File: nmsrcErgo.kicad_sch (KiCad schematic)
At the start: 56 parts, among them SW1 RotaryEncoder_Switch, U1 Nice_Nano_V2

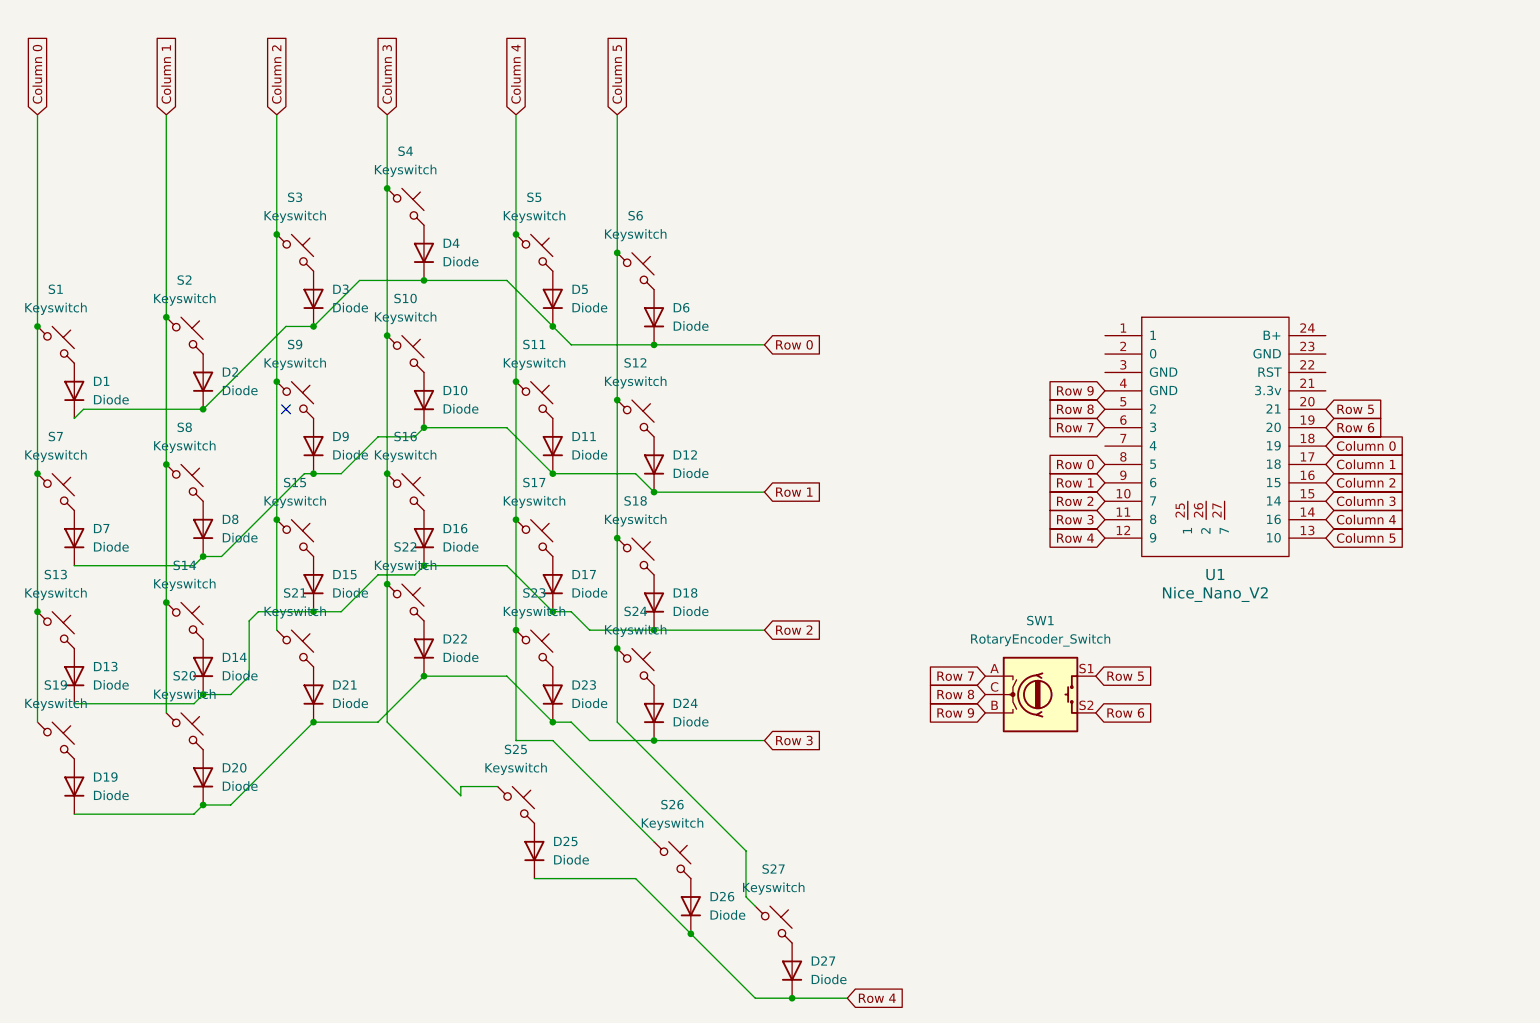
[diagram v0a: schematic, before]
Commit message: on/off switch and fixed encoder. added battery solder pads
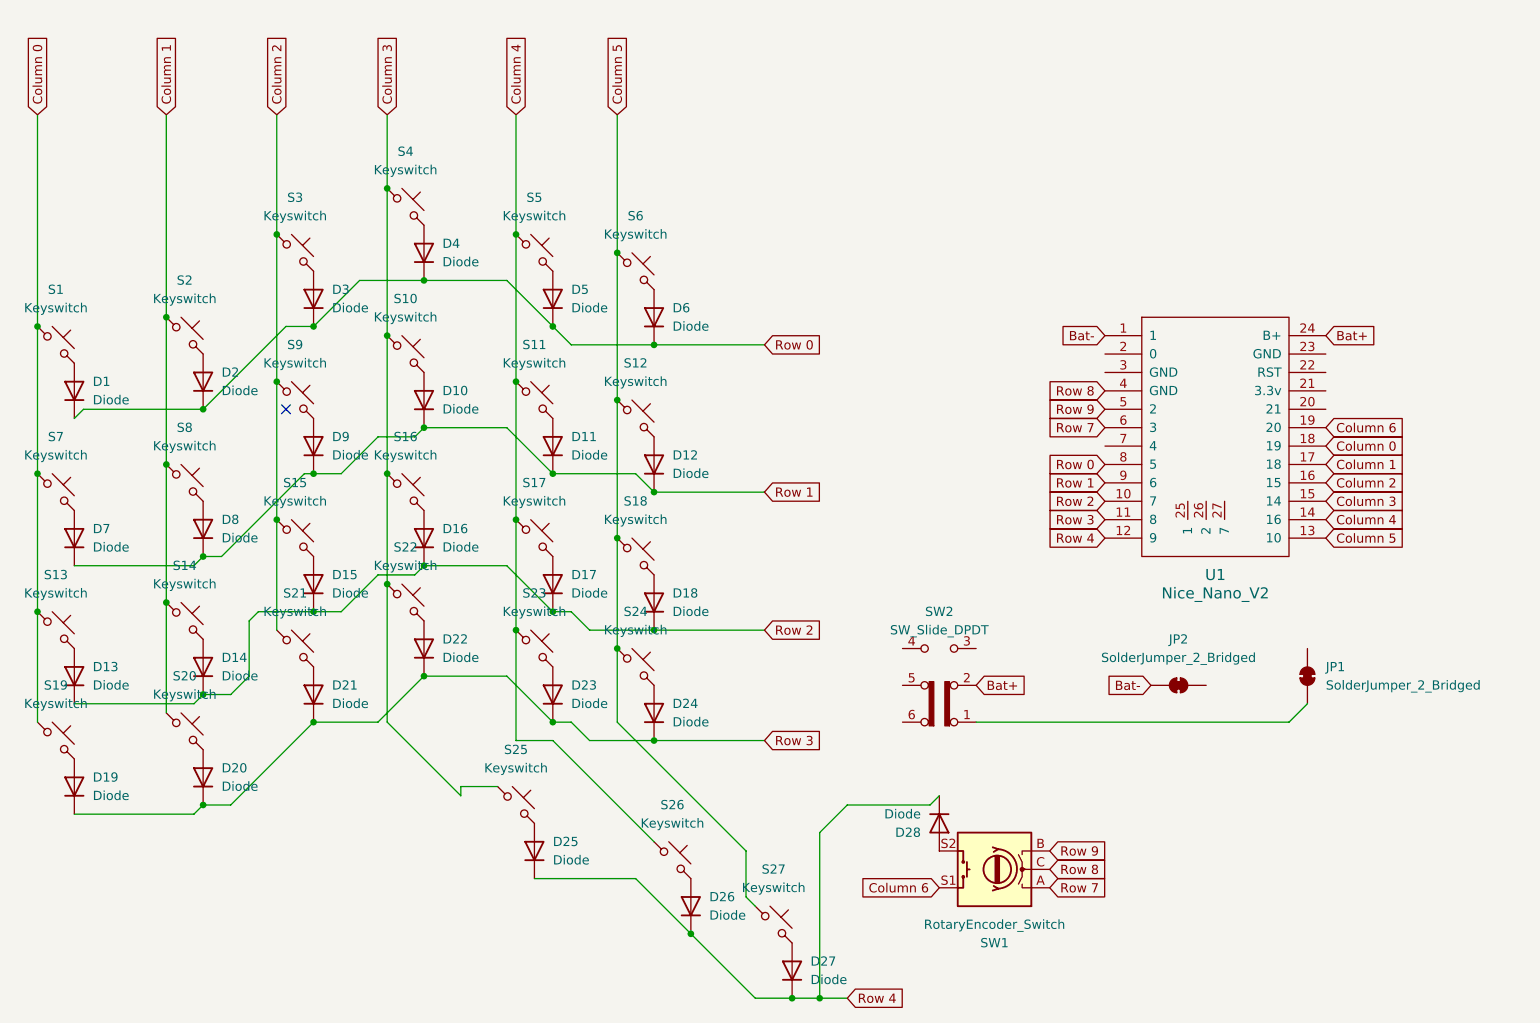
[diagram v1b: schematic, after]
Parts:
- added D28: Diode, ScottoKeebs_Components:Diode_DO-35, symbol ScottoKeebs:Placeholder_Diode
- added JP1, JP2: SolderJumper_2_Bridged, ScottoKeebs_Miscellaneous:solderpadv2, symbol Jumper:SolderJumper_2_Bridged
- added SW2: SW_Slide_DPDT, Button_Switch_THT:SW_Slide-03_Wuerth-WS-SLTV_10x2.5x6.4_P2.54mm, symbol Switch:SW_Slide_DPDT
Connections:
- net Row 4: now also D28.1 (K)
- net Row 8: now also U1.4 (GND); no longer U1.5 (2)
- net Row 9: now also U1.5 (2); no longer U1.4 (GND)
- net Bat-: now reaches U1.1
- net Bat-: now also JP2.1 (A)
- net Bat+: now reaches U1.24 (B+)
- net Bat+: now also SW2.2 (B)
- net Row 5: no longer names the net of U1.20 (21)
- net Row 5: no longer SW1.S1
- net Row 6: no longer names the net of SW1.S2
- net Row 6: now also D28.2 (A); no longer U1.19 (20)
- new net: JP1.1 (A), SW2.1 (A)
- new net Column 6: SW1.S1, U1.19 (20)
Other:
- moved on the sheet: SW1
